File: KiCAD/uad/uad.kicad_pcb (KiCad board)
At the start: 2 copper layers, 50 x 50 mm, 0 parts

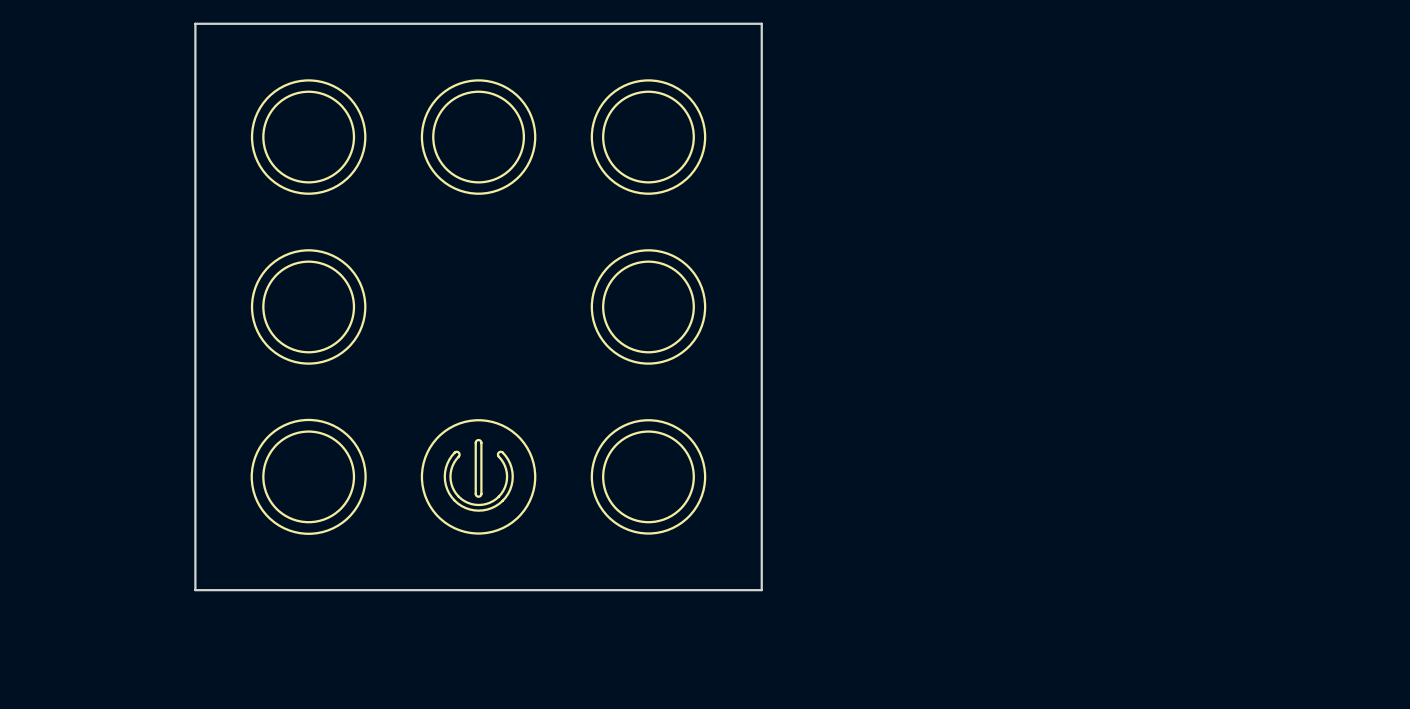
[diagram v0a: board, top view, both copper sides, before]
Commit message: трассировка
не расставлены резисторы/конденсатор емкостных кнопок
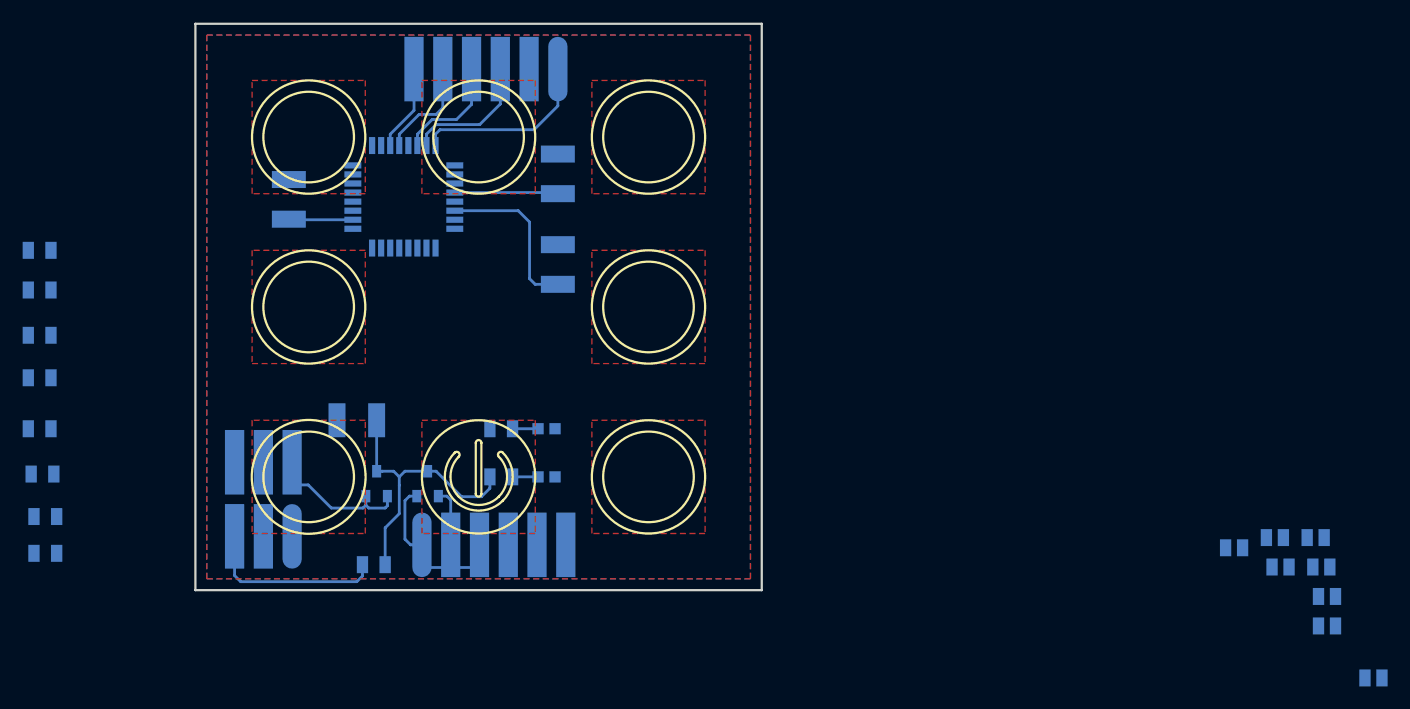
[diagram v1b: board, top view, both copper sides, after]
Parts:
- added C1: 12пФ(0603), N_RLC:Конденсатор_SMD_0603, B.Cu at (193.2, 102.8)
- added C10: 4.7мкФ(1210), N_RLC:Конденсатор_SMD_1210, B.Cu at (122.0, 56.5)
- added C11: 4.7мкФ(1210), N_RLC:Конденсатор_SMD_1210, B.Cu at (122.0, 64.5)
- added C12: 4.7мкФ(1210), N_RLC:Конденсатор_SMD_1210, B.Cu at (102.5, 80.0)
- added C2: 12пФ(0603), N_RLC:Конденсатор_SMD_0603, B.Cu at (188.2, 90.4)
- added C3: 12пФ(0603), N_RLC:Конденсатор_SMD_0603, B.Cu at (188.7, 93.0)
- added C4: 12пФ(0603), N_RLC:Конденсатор_SMD_0603, B.Cu at (184.6, 90.4)
- added C5: 12пФ(0603), N_RLC:Конденсатор_SMD_0603, B.Cu at (189.2, 95.6)
- added C6: 12пФ(0603), N_RLC:Конденсатор_SMD_0603, B.Cu at (185.1, 93.0)
- added C7: 12пФ(0603), N_RLC:Конденсатор_SMD_0603, B.Cu at (189.2, 98.2)
- added C8: 12пФ(0603), N_RLC:Конденсатор_SMD_0603, B.Cu at (181.0, 91.3)
- added C9: 4.7мкФ(1210), N_RLC:Конденсатор_SMD_1210, B.Cu at (98.2, 58.8)
- added DD1: ATmega8A-AU, N_DD:микросхема_ATMEGA-8-161AU, B.Cu at (112.7, 57.5)
- added HL1: Светодиод, N_VD_HL:Светодиод_SMD_0603, B.Cu at (120.2, 85.0)
- added HL2: Светодиод, N_VD_HL:Светодиод_SMD_0603, B.Cu at (120.2, 80.8)
- added R1: 2 МОм(0805), N_RLC:Резистор_SMD_0805_0,125Вт, B.Cu at (75.2, 65.0)
- added R10: 100 Ом(0805), N_RLC:Резистор_SMD_0805_0,125Вт, B.Cu at (116.0, 85.0)
- added R11: 100 Ом(0805), N_RLC:Резистор_SMD_0805_0,125Вт, B.Cu at (116.0, 80.8)
- added R2: 2 МОм(0805), N_RLC:Резистор_SMD_0805_0,125Вт, B.Cu at (75.2, 68.5)
- added R3: 2 МОм(0805), N_RLC:Резистор_SMD_0805_0,125Вт, B.Cu at (75.2, 72.5)
- added R4: 2 МОм(0805), N_RLC:Резистор_SMD_0805_0,125Вт, B.Cu at (75.2, 76.2)
- added R5: 2 МОм(0805), N_RLC:Резистор_SMD_0805_0,125Вт, B.Cu at (75.2, 80.8)
- added R6: 2 МОм(0805), N_RLC:Резистор_SMD_0805_0,125Вт, B.Cu at (75.5, 84.8)
- added R7: 2 МОм(0805), N_RLC:Резистор_SMD_0805_0,125Вт, B.Cu at (75.8, 88.5)
- added R8: 2 МОм(0805), N_RLC:Резистор_SMD_0805_0,125Вт, B.Cu at (75.8, 91.8)
- added R9: 20 кОм(0805), N_RLC:Резистор_SMD_0805_0,125Вт, B.Cu at (104.8, 92.8)
- added VD1: Диод_шоттки, N_VD_HL:Диод_BAR43CFILM_SOT-23, B.Cu at (110.5, 85.6)
- added VD2: Диод_шоттки, N_VD_HL:Диод_BAR43CFILM_SOT-23, B.Cu at (106.0, 85.6)
- added XP1: Вилка_PLS6, N_X:Вилка_PLS6_угловая_вертикальная, B.Cu at (110.0, 93.0)
- added XP2: Вилка_PLS6, N_X:Вилка_PLS6_угловая_вертикальная, B.Cu at (122.0, 47.0)
- added XP3: Вилка_PLD6_ПРОГ, N_X:Вилка_PLD6_угловая_вертикальная, B.Cu at (98.5, 88.2)
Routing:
- net VCC: track 0.00 -> 55.0 mm
- net Net-(VD1-Pad1): track 0.00 -> 20.2 mm
- net RES: track 0.00 -> 18.2 mm
- net NeoPixel_OUT: track 0.00 -> 18.1 mm
- net TX: track 0.00 -> 13.7 mm
- net RX: track 0.00 -> 12.0 mm
- net PWM_OUT_2: track 0.00 -> 11.2 mm
- net Net-(VD2-Pad1): track 0.00 -> 11.2 mm
- net PWM_OUT_1: track 0.00 -> 9.62 mm
- net Net-(HL2-Pad1): track 0.00 -> 2.25 mm
- net Net-(HL1-Pad1): track 0.00 -> 2.25 mm
- added copper zone on F.Cu, net BUT_0_CUP
- added copper zone on F.Cu, net BUT_1_CUP
- added copper zone on F.Cu, net BUT_2_CUP
- added copper zone on F.Cu, net BUT_3_CUP
- added copper zone on F.Cu, net BUT_4_CUP
- added copper zone on F.Cu, net BUT_5_CUP
- added copper zone on F.Cu, net BUT_6_CUP
- added copper zone on F.Cu, net BUT_7_CUP
- added copper zone on F.Cu, net BUT_COM_OUT
- added copper zone on B.Cu, net GND
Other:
- net class button added: clearance 0.2, trace_width 0.45, via_dia 1.2, via_drill 0.7

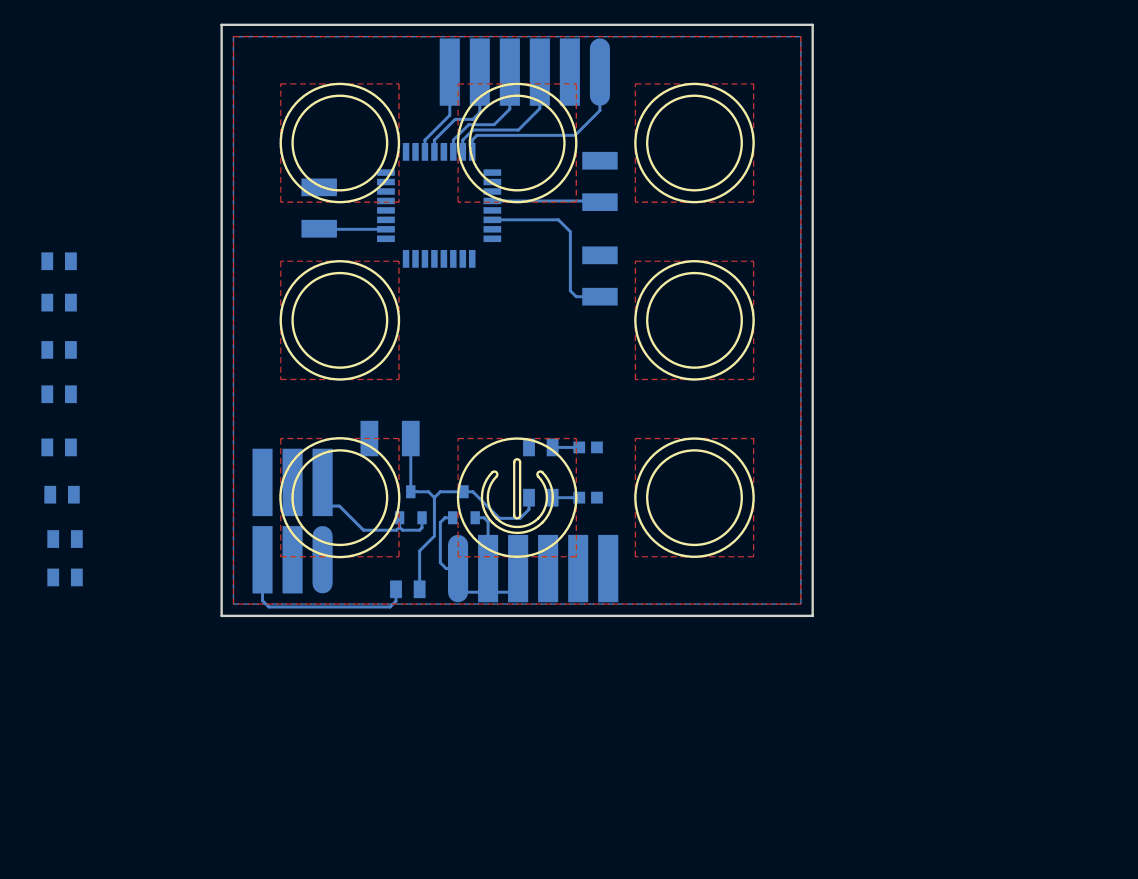
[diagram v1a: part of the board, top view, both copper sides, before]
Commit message: переделана схема
программирование совмещено с питанием
выход на общую плату - дискретные выхода
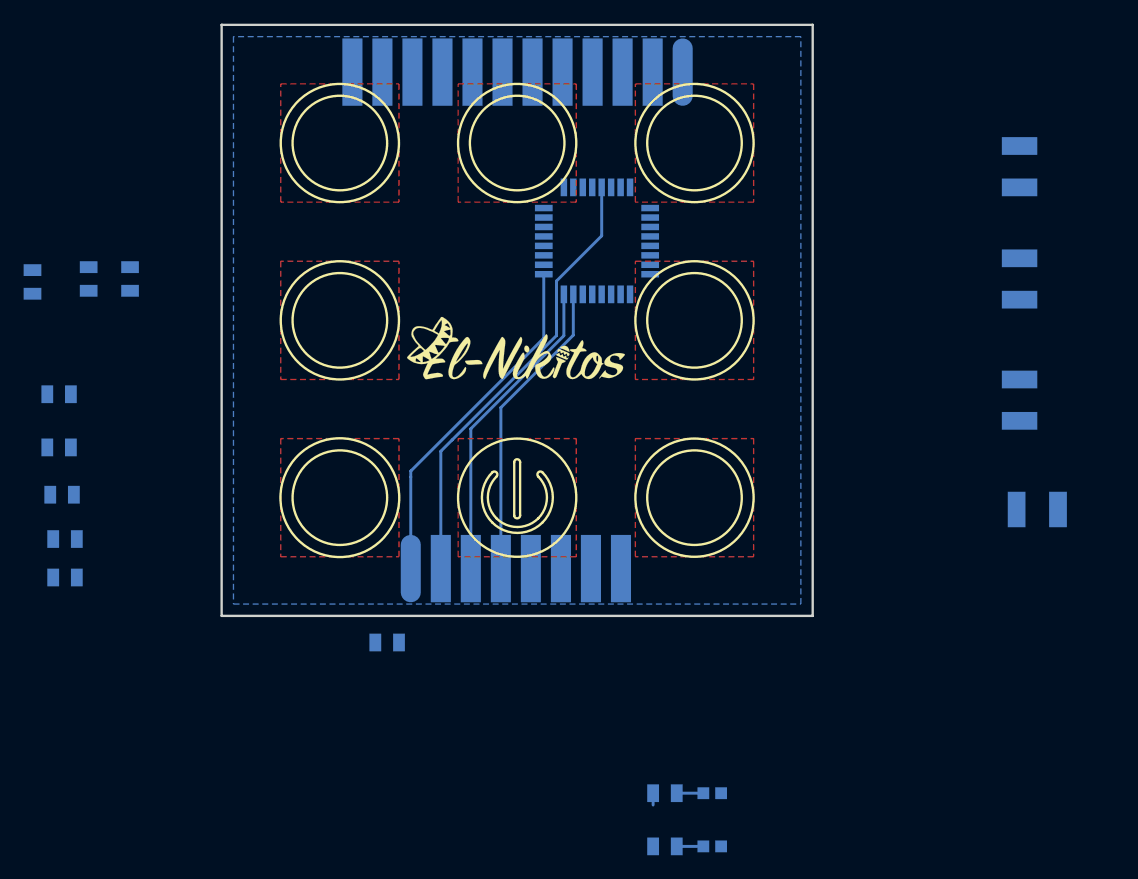
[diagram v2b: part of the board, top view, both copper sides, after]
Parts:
- removed VD1, VD2: Диод_шоттки, N_VD_HL:Диод_BAR43CFILM_SOT-23
- removed XP3: Вилка_PLD6_ПРОГ, N_X:Вилка_PLD6_угловая_вертикальная
- added G***: LOGO, N_ICO:el-nikitos_19x7, F.Cu at (115.2, 72.8)
- XP1: value Вилка_PLS6 -> Вилка_PLS8; footprint N_X:Вилка_PLS6_угловая_вертикальная -> N_X:Вилка_PLS8_угловая_вертикальная
- XP2: value Вилка_PLS6 -> Вилка_PLS12; footprint N_X:Вилка_PLS6_угловая_вертикальная -> N_X:Вилка_PLS12_угловая_вертикальная
- moved C9 61.4 mm to (157.5, 75.0)
- moved C12 55.1 mm to (157.2, 86.0)
- moved C10 35.5 mm to (157.5, 55.2)
- moved C11 35.5 mm to (157.5, 64.8)
- moved HL2 35.3 mm to (130.8, 114.5)
- moved R11 35.3 mm to (126.5, 114.5)
- moved HL1 27.1 mm to (130.8, 110.0)
- moved R10 27.1 mm to (126.5, 110.0)
- moved DD1 13.7 mm to (126.0, 60.5)
- moved R3 9.90 mm to (82.2, 65.5), turned to 270 degrees
- moved XP2 7.00 mm to (129.0, 47.0)
- moved R9 4.83 mm to (103.0, 97.2)
- moved XP1 4.00 mm to (106.0, 93.0)
- moved R1 3.54 mm to (78.8, 65.5), turned to 270 degrees
- moved R2 3.02 mm to (74.0, 65.8), turned to 270 degrees
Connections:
- net Net-(XP2-Pad2) renamed D_Out_2
- DD1 pad 1: BUT_3_CUP -> Net-(DD1-Pad1)
- DD1 pad 10: BUT_6_CUP -> Net-(DD1-Pad10)
- DD1 pad 11: BUT_7_CUP -> Net-(DD1-Pad11)
- DD1 pad 12: BUT_COM_OUT -> Net-(DD1-Pad12)
- DD1 pad 13: Net-(DD1-Pad13) -> PWM_OUT_1
- DD1 pad 14: Net-(DD1-Pad14) -> PWM_OUT_2
- DD1 pad 2: BUT_4_CUP -> Net-(DD1-Pad2)
- DD1 pad 23: BUT_0_CUP -> Net-(DD1-Pad23)
- DD1 pad 24: BUT_1_CUP -> Net-(DD1-Pad24)
- DD1 pad 25: BUT_2_CUP -> Net-(DD1-Pad25)
- DD1 pad 26: LED_work -> Net-(DD1-Pad26)
- DD1 pad 27: PWM_OUT_1 -> Net-(DD1-Pad27)
- DD1 pad 28: PWM_OUT_2 -> Net-(DD1-Pad28)
- DD1 pad 32: NeoPixel_OUT -> Net-(DD1-Pad32)
- DD1 pad 9: BUT_5_CUP -> Net-(DD1-Pad9)
- R9 pad 1: RES -> VCC
- R9 pad 2: VCC -> RES
- XP1 pad 1: Net-(VD1-Pad1) -> SCK
- XP1 pad 2: Net-(VD1-Pad1) -> RES
- XP1 pad 3: Net-(VD1-Pad1) -> MISO
- XP1 pad 4: GND -> MOSI
- XP1 pad 5: GND -> VCC
- XP1 pad 6: GND -> VCC
- XP2 pad 1: NeoPixel_OUT -> D_Out_1
- XP2 pad 3: TX -> D_Out_3
- XP2 pad 4: RX -> D_Out_4
- XP2 pad 5: PWM_OUT_2 -> D_Out_5
- XP2 pad 6: PWM_OUT_1 -> D_Out_6
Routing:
- net VCC: track 55.0 -> 1.00 mm
- net SCK: track 0.00 -> 31.6 mm
- net MISO: track 0.00 -> 28.5 mm
- net MOSI: track 0.00 -> 27.7 mm
- net RES: track 18.2 -> 39.9 mm
- net Net-(VD1-Pad1): track 20.2 -> 0.00 mm
- net NeoPixel_OUT: track 18.1 -> 0.00 mm
- net TX: track 13.7 -> 0.00 mm
- net RX: track 12.0 -> 0.00 mm
- net PWM_OUT_2: track 11.2 -> 0.00 mm
- net Net-(VD2-Pad1): track 11.2 -> 0.00 mm
- net PWM_OUT_1: track 9.62 -> 0.00 mm
- removed copper zone on F.Cu, net BUT_COM_OUT
